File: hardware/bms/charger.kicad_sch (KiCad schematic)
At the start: 67 parts, among them Q7 BSZ018N04LS6ATMA1, Q8 BSZ018N04LS6ATMA1, Q9 BSZ018N04LS6ATMA1, U2 LM74700, U3 BQ24610

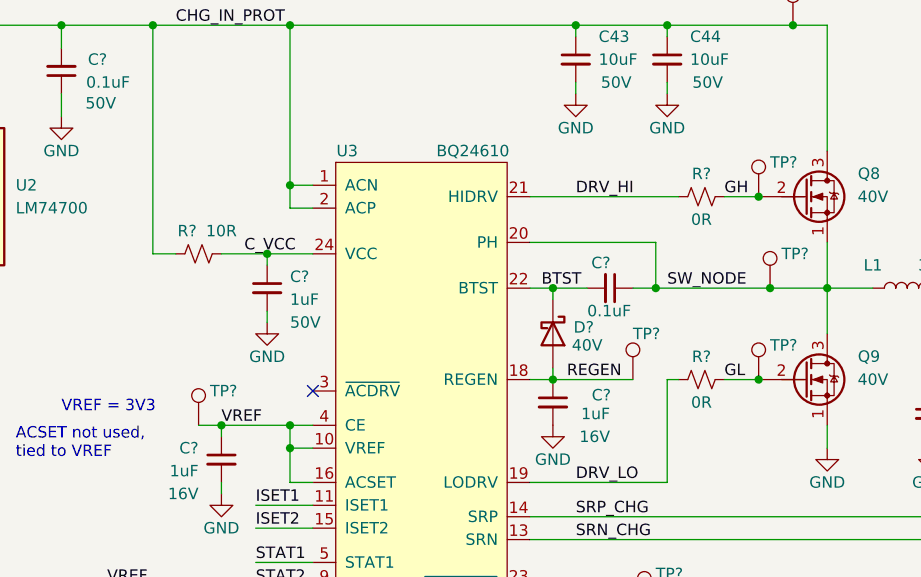
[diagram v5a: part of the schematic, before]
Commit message: Changed large input fuse, slightly smaller and cheaper, 60A rated. Layout more defined, charger layout much better now
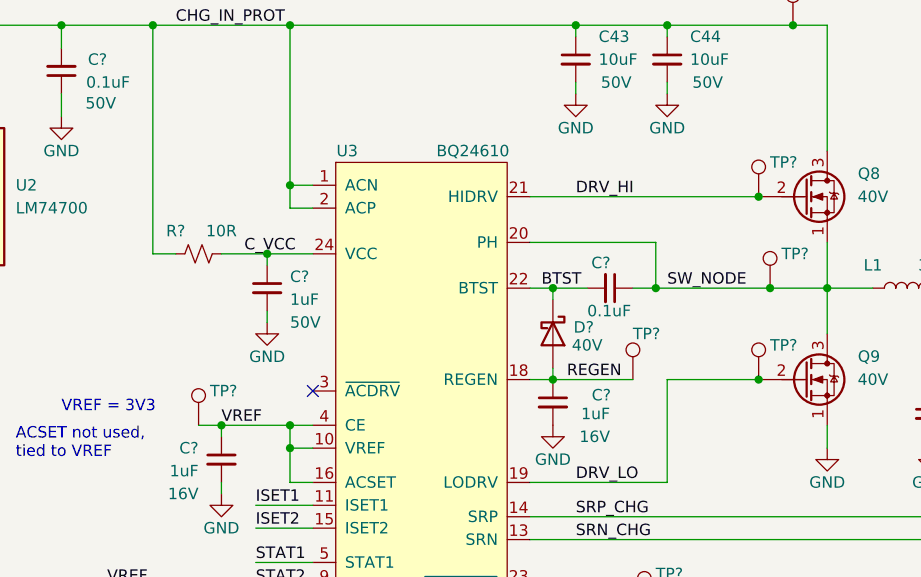
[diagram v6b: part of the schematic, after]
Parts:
- removed R? (x2): 0R, Resistor_SMD:R_0603_1608Metric, symbol Device:R_Small_US
- C?: footprint Capacitor_SMD:C_0805_2012Metric -> Capacitor_SMD:C_0603_1608Metric; MFG PN GCM21BR71H105KA03K -> GRT188R61H105KE13D
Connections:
- net GH is gone; now on net DRV_HI: Q8.2 (G), TP?.1
- net GL is gone; now on net DRV_LO: Q9.2 (G), TP?.1
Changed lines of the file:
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@@
     (stroke (width 0) (type default))
   )
-  (wire (pts (xy 177.8 55.88) (xy 181.61 55.88))
-    (stroke (width 0) (type default))
-  )
   (wire (pts (xy 262.89 101.6) (xy 262.89 105.41))
     (stroke (width 0) (type default))
@@
     (stroke (width 0) (type default))
   )
-  (wire (pts (xy 156.21 55.88) (xy 172.72 55.88))
+  (wire (pts (xy 156.21 55.88) (xy 181.61 55.88))
     (stroke (width 0) (type default))
   )
@@
     (stroke (width 0) (type default))
   )
-  (wire (pts (xy 177.8 76.2) (xy 181.61 76.2))
-    (stroke (width 0) (type default))
-  )
   (wire (pts (xy 121.92 148.59) (xy 121.92 146.05))
     (stroke (width 0) (type default))
@@
     (stroke (width 0) (type default))
   )
-  (wire (pts (xy 171.45 76.2) (xy 172.72 76.2))
+  (wire (pts (xy 171.45 76.2) (xy 181.61 76.2))
     (stroke (width 0) (type default))
   )
@@
     (effects (font (size 1.27 1.27)) (justify left bottom))
   )
-  (label "GL" (at 177.8 76.2 0) (fields_autoplaced)
-    (effects (font (size 1.27 1.27)) (justify left bottom))
-  )
   (label "STAT1" (at 125.73 96.52 0) (fields_autoplaced)
     (effects (font (size 1.27 1.27)) (justify left bottom))
@@
     (effects (font (size 1.27 1.27)) (justify left bottom))
   )
-  (label "GH" (at 177.8 55.88 0) (fields_autoplaced)
-    (effects (font (size 1.27 1.27)) (justify left bottom))
-  )
   (label "VREF" (at 29.21 146.05 0) (fields_autoplaced)
     (effects (font (size 1.27 1.27)) (justify left bottom))
@@
       (effects (font (size 1.27 1.27)) (justify left))
     )
-    (property "Footprint" "Capacitor_SMD:C_0805_2012Metric" (at 127 66.04 0)
+    (property "Footprint" "Capacitor_SMD:C_0603_1608Metric" (at 127 66.04 0)
       (effects (font (size 1.27 1.27)) hide)
     )
@@
       (effects (font (size 1.27 1.27)) hide)
     )
-    (property "MFG PN" "GCM21BR71H105KA03K" (at 127 66.04 0)
+    (property "MFG PN" "GRT188R61H105KE13D" (at 127 66.04 0)
       (effects (font (size 1.27 1.27)) hide)
     )
@@
     )
   )
-  (symbol (lib_id "Device:R_Small_US") (at 175.26 55.88 90) (unit 1)
-    (in_bom yes) (on_board yes) (dnp no)
-    (property "Reference" "R?" (at 175.26 53.34 90)
-      (effects (font (size 1.27 1.27)))
-    )
-    (property "Value" "0R" (at 175.26 58.42 90)
-      (effects (font (size 1.27 1.27)))
-    )
-    (property "Footprint" "Resistor_SMD:R_0603_1608Metric" (at 175.26 55.88 0)
-      (effects (font (size 1.27 1.27)) hide)
-    )
-    (property "Datasheet" "~" (at 175.26 55.88 0)
-      (effects (font (size 1.27 1.27)) hide)
-    )
-    (property "MFG" "Panasonic Electronic Components" (at 175.26 55.88 90)
-      (effects (font (size 1.27 1.27)) hide)
-    )
-    (property "MFG PN" "ERJ-3GEY0R00V" (at 175.26 55.88 90)
-      (effects (font (size 1.27 1.27)) hide)
-    )
-    (pin "1")
-    (pin "2")
-    (instances
-      (project "bms"
-        (path "/a4805e9d-b940-444e-a7cb-db4f4c53ed46/00000000-0000-0000-0000-00006523a805"
-          (reference "R?") (unit 1)
-        )
-        (path "/a4805e9d-b940-444e-a7cb-db4f4c53ed46/00000000-0000-0000-0000-00006523ab32"
-          (reference "R43") (unit 1)
-        )
-      )
-    )
-  )
   (symbol (lib_id "power:GND") (at 40.64 123.19 0) (unit 1)
     (in_bom yes) (on_board yes) (dnp no)
@@
     )
   )
-  (symbol (lib_id "Device:R_Small_US") (at 175.26 76.2 90) (unit 1)
-    (in_bom yes) (on_board yes) (dnp no)
-    (property "Reference" "R?" (at 175.26 73.66 90)
-      (effects (font (size 1.27 1.27)))
-    )
-    (property "Value" "0R" (at 175.26 78.74 90)
-      (effects (font (size 1.27 1.27)))
-    )
-    (property "Footprint" "Resistor_SMD:R_0603_1608Metric" (at 175.26 76.2 0)
-      (effects (font (size 1.27 1.27)) hide)
-    )
-    (property "Datasheet" "~" (at 175.26 76.2 0)
-      (effects (font (size 1.27 1.27)) hide)
-    )
-    (property "MFG" "Panasonic Electronic Components" (at 175.26 76.2 90)
-      (effects (font (size 1.27 1.27)) hide)
-    )
-    (property "MFG PN" "ERJ-3GEY0R00V" (at 175.26 76.2 90)
-      (effects (font (size 1.27 1.27)) hide)
-    )
-    (pin "1")
-    (pin "2")
-    (instances
-      (project "bms"
-        (path "/a4805e9d-b940-444e-a7cb-db4f4c53ed46/00000000-0000-0000-0000-00006523a805"
-          (reference "R?") (unit 1)
-        )
-        (path "/a4805e9d-b940-444e-a7cb-db4f4c53ed46/00000000-0000-0000-0000-00006523ab32"
-          (reference "R46") (unit 1)
-        )
-      )
-    )
-  )
   (symbol (lib_id "Device:C_Small") (at 68.58 46.99 180) (unit 1)
     (in_bom yes) (on_board yes) (dnp no)
@@
   (symbol (lib_id "Device:R_Small_US") (at 119.38 62.23 90) (unit 1)
     (in_bom yes) (on_board yes) (dnp no)
-    (property "Reference" "R?" (at 118.11 59.69 90)
+    (property "Reference" "R?" (at 116.84 59.69 90)
       (effects (font (size 1.27 1.27)))
     )

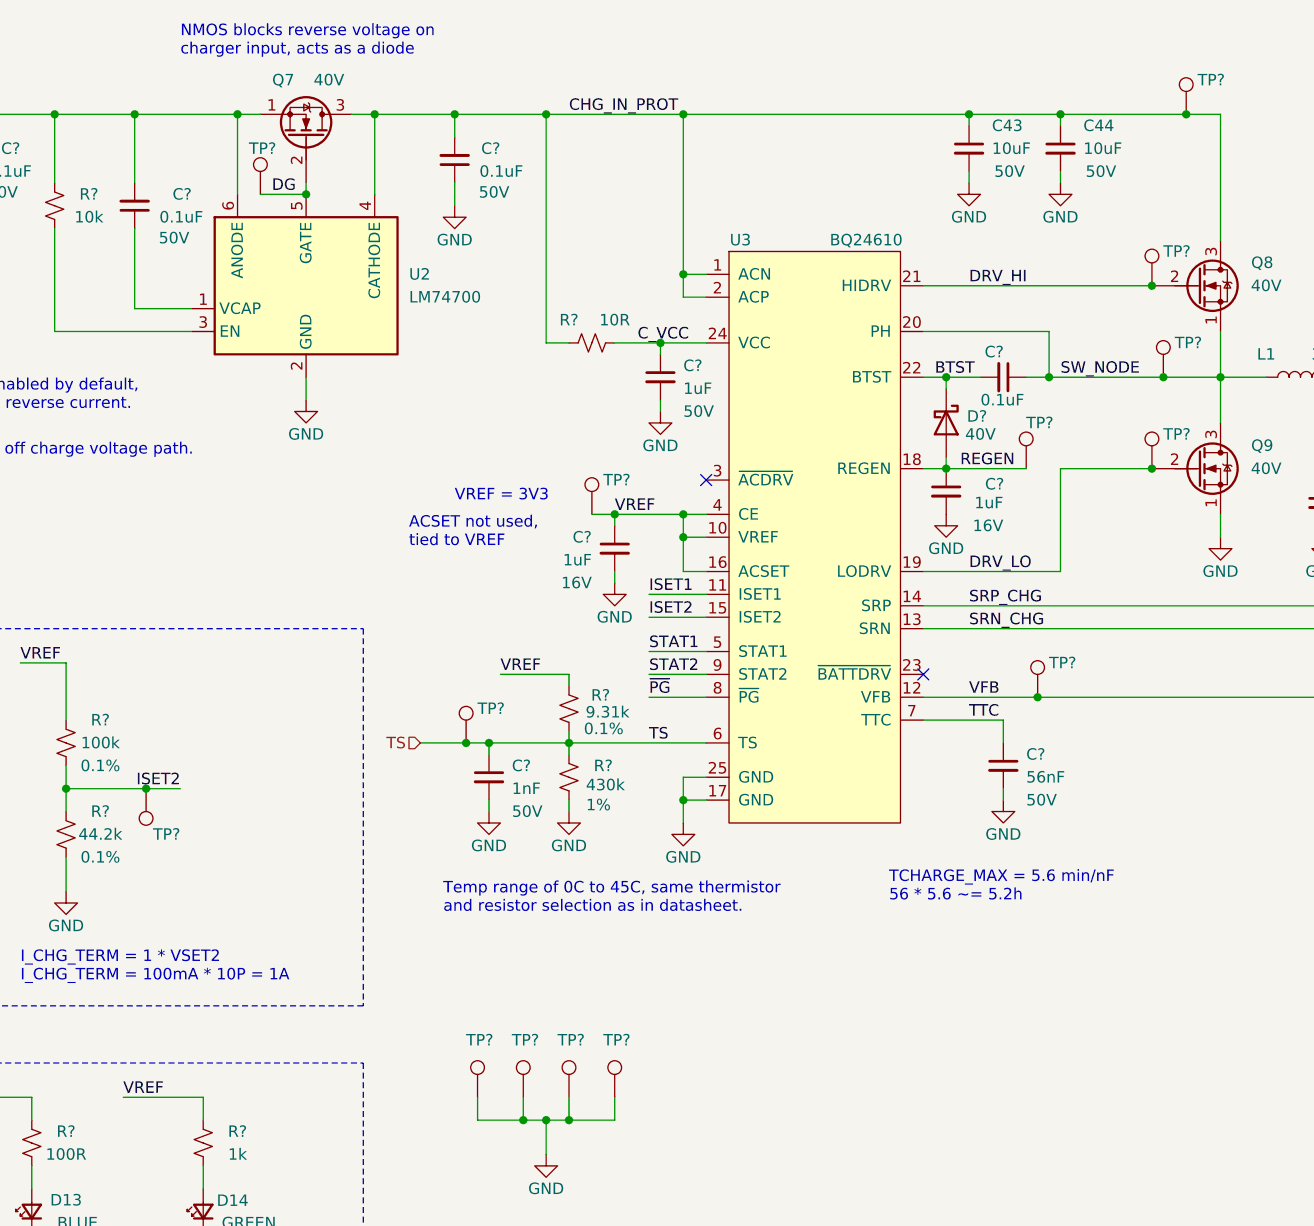
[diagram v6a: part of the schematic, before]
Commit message: Review of BMS board looks good, finished!
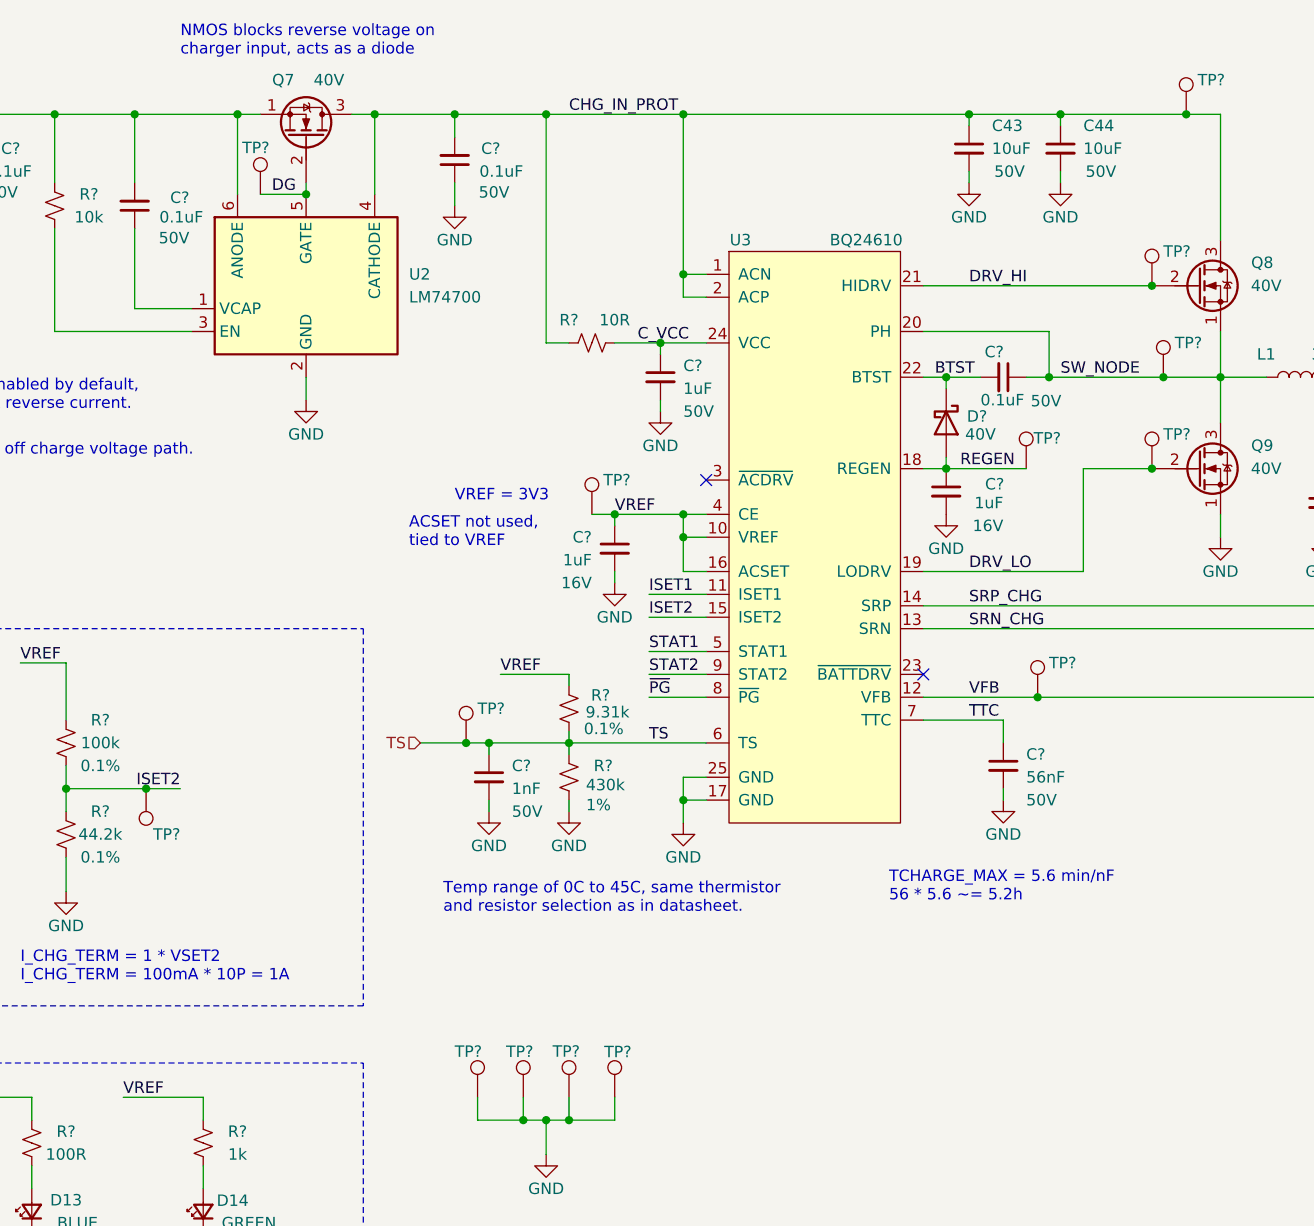
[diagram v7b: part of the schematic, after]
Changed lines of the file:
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@@
     (stroke (width 0) (type default))
   )
-  (wire (pts (xy 156.21 87.63) (xy 171.45 87.63))
+  (wire (pts (xy 156.21 87.63) (xy 173.99 87.63))
     (stroke (width 0) (type default))
   )
@@
     (stroke (width 0) (type default))
   )
-  (wire (pts (xy 171.45 87.63) (xy 171.45 76.2))
+  (wire (pts (xy 173.99 87.63) (xy 173.99 76.2))
     (stroke (width 0) (type default))
   )
@@
     (stroke (width 0) (type default))
   )
-  (wire (pts (xy 171.45 76.2) (xy 181.61 76.2))
+  (wire (pts (xy 173.99 76.2) (xy 181.61 76.2))
     (stroke (width 0) (type default))
   )
@@
   (symbol (lib_id "Connector:TestPoint") (at 106.68 146.05 0) (unit 1)
     (in_bom no) (on_board yes) (dnp no)
-    (property "Reference" "TP?" (at 105.41 139.7 0)
+    (property "Reference" "TP?" (at 104.14 140.97 0)
       (effects (font (size 1.27 1.27)) (justify left))
     )
@@
       (effects (font (size 1.27 1.27)) hide)
     )
-    (property "Voltage" "50V" (at 163.83 69.85 90)
-      (effects (font (size 1.27 1.27)) (justify left) hide)
+    (property "Voltage" "50V" (at 168.1362 68.6883 90)
+      (effects (font (size 1.27 1.27)) (justify left))
     )
     (pin "1")
@@
   (symbol (lib_id "Connector:TestPoint") (at 116.84 146.05 0) (unit 1)
     (in_bom no) (on_board yes) (dnp no)
-    (property "Reference" "TP?" (at 115.57 139.7 0)
+    (property "Reference" "TP?" (at 115.0182 140.9573 0)
       (effects (font (size 1.27 1.27)) (justify left))
     )
@@
   (symbol (lib_id "Connector:TestPoint") (at 121.92 146.05 0) (unit 1)
     (in_bom no) (on_board yes) (dnp no)
-    (property "Reference" "TP?" (at 120.65 139.7 0)
+    (property "Reference" "TP?" (at 120.7522 141.0063 0)
       (effects (font (size 1.27 1.27)) (justify left))
     )
@@
   (symbol (lib_id "Device:C_Small") (at 68.58 46.99 180) (unit 1)
     (in_bom yes) (on_board yes) (dnp no)
-    (property "Reference" "C?" (at 74.93 45.72 0)
+    (property "Reference" "C?" (at 74.6651 46.0913 0)
       (effects (font (size 1.27 1.27)) (justify left))
     )
@@
   (symbol (lib_id "Connector:TestPoint") (at 111.76 146.05 0) (unit 1)
     (in_bom no) (on_board yes) (dnp no)
-    (property "Reference" "TP?" (at 110.49 139.7 0)
+    (property "Reference" "TP?" (at 109.8477 140.9818 0)
       (effects (font (size 1.27 1.27)) (justify left))
     )
@@
   (symbol (lib_id "Connector:TestPoint") (at 167.64 76.2 0) (unit 1)
     (in_bom no) (on_board yes) (dnp no)
-    (property "Reference" "TP?" (at 167.64 71.12 0)
+    (property "Reference" "TP?" (at 168.467 72.8234 0)
       (effects (font (size 1.27 1.27)) (justify left))
     )
@@
   (symbol (lib_id "Connector:TestPoint") (at 82.55 45.72 0) (unit 1)
     (in_bom no) (on_board yes) (dnp no)
-    (property "Reference" "TP?" (at 81.28 40.64 0)
+    (property "Reference" "TP?" (at 80.5245 40.5537 0)
       (effects (font (size 1.27 1.27)) (justify left))
     )
